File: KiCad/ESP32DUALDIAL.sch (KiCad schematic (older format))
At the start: 53 parts, among them J1 SERVICE, J2 Conn_01x04_Male, J5 Conn_01x03_Male, J6 Conn_01x02_Male, J7 Conn_01x02_Male, J8 Conn_01x02_Male, M1 Fan_CPU_4pin, M2 Fan_CPU_4pin, Q1 Q_NMOS_GDS, SW1 Rotary_Encoder_Switch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

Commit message: change to ROTARY ENCODER chattaling fix. and many change...
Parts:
- added R11, R12, R13, R14, R15, R16: 270, Resistor_SMD:R_0603_1608Metric, symbol Device:R
- added R17, R18, R19, R20, R21, R22: 10k, Resistor_SMD:R_0603_1608Metric, symbol Device:R
- R3: value 4.7k -> 10k
- R5, R6, R7, R8: value 330 -> 270
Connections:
- net +3V3: now also R17.1, R18.1, R19.1, R20.1, R21.1, R22.1
- net OZON0: now also U2.11 (IO26); no longer U2.33 (IO21)
- net PUMP: now also U2.12 (IO27); no longer R1.2, U2.23 (IO15), U4.2 (IO)
- net at C8.1, SW1.A: now also R13.1; no longer U2.12 (IO27)
- net at C9.1, SW1.B: now also R12.1; no longer U2.11 (IO26)
- net at C4.1, SW1.S2: now also R11.1; no longer U2.10 (IO25)
- net at C12.1, SW2.S2: now also R14.1; no longer U2.13 (IO14)
- net at C7.1, SW2.B: now also R15.1; no longer U2.14 (IO12)
- net at C5.1, SW2.A: now also R16.1; no longer U2.16 (IO13)
- net at U2.6 (IO34): now also R12.2, R18.2
- net at U2.7 (IO35): now also R13.2, R20.2
- new net: R1.2, U2.23 (IO15), U4.2 (IO)
- new net: R11.2, R17.2, U2.10 (IO25)
- new net: R14.2, R22.2, U2.13 (IO14)
- new net: R15.2, R19.2, U2.14 (IO12)
- new net: R16.2, R21.2, U2.16 (IO13)
- no-connect marks 30 -> 28
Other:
- moved on the sheet: C5, C7, C8, C9

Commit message: Ver.6 : Add test pads / NNC and SHARP SSR both support / mode jumper
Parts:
- added J3: mode, Connector_PinHeader_2.54mm:PinHeader_2x01_P2.54mm_Vertical, symbol Connector_Generic:Conn_01x02
- added TP1, TP10, TP11, TP12, TP2, TP3, TP4, TP5, TP6, TP8, TP9: TestPoint, TestPoint:TestPoint_Pad_D2.0mm, symbol Connector:TestPoint
- added TP13, TP7: TestPoint, TestPoint:TestPoint_Pad_D3.0mm, symbol Connector:TestPoint
- BZ1: footprint Buzzer_Beeper:Buzzer_12x9.5RM7.6 -> library:Buzzer_7.6_5.0
- U5, U6, U7, U8: footprint library:SSR_SHARP_S108T02 -> library:SSR_SHARP_S108T02_NNC_NNG1D-25mm
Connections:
- net +12V: now also TP13.1
- net +3V3: now also TP7.1
- net GND: now also J3.1 (Pin_1)
- net at R11.2, R17.2, U2.10 (IO25): now also TP1.1
- net at R14.2, R22.2, U2.13 (IO14): now also TP4.1
- net at R15.2, R19.2, U2.14 (IO12): now also TP5.1
- net at R16.2, R21.2, U2.16 (IO13): now also TP6.1
- net at U2.33 (IO21): now also J3.2 (Pin_2)
- net at R12.2, R18.2, U2.6 (IO34): now also TP2.1
- net at R13.2, R20.2, U2.7 (IO35): now also TP3.1
- net at R5.1, U5.3: now also TP9.1
- net at R6.1, U6.3: now also TP10.1
- net at R7.1, U7.3: now also TP11.1
- net at R8.1, U8.3: now also TP12.1
- net at C11.1, D1.2 (A), M1.1 (-)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: now also TP8.1
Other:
- note added: "DO NOT USE R19"
- note added: "SENSOR_VP is GPIO36\nSENSOR_VN is GPIO39\nIO34 to IO39 are input only\nBoot mode is GPIO0,2,4,5,12,15"
- note added: "normally 12V"
- note removed: "IO34,IO35 is input only"
- moved on the sheet: F1, J2, J5, J6, J7, J8, PS1, R5, R6, R7, R8, U5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

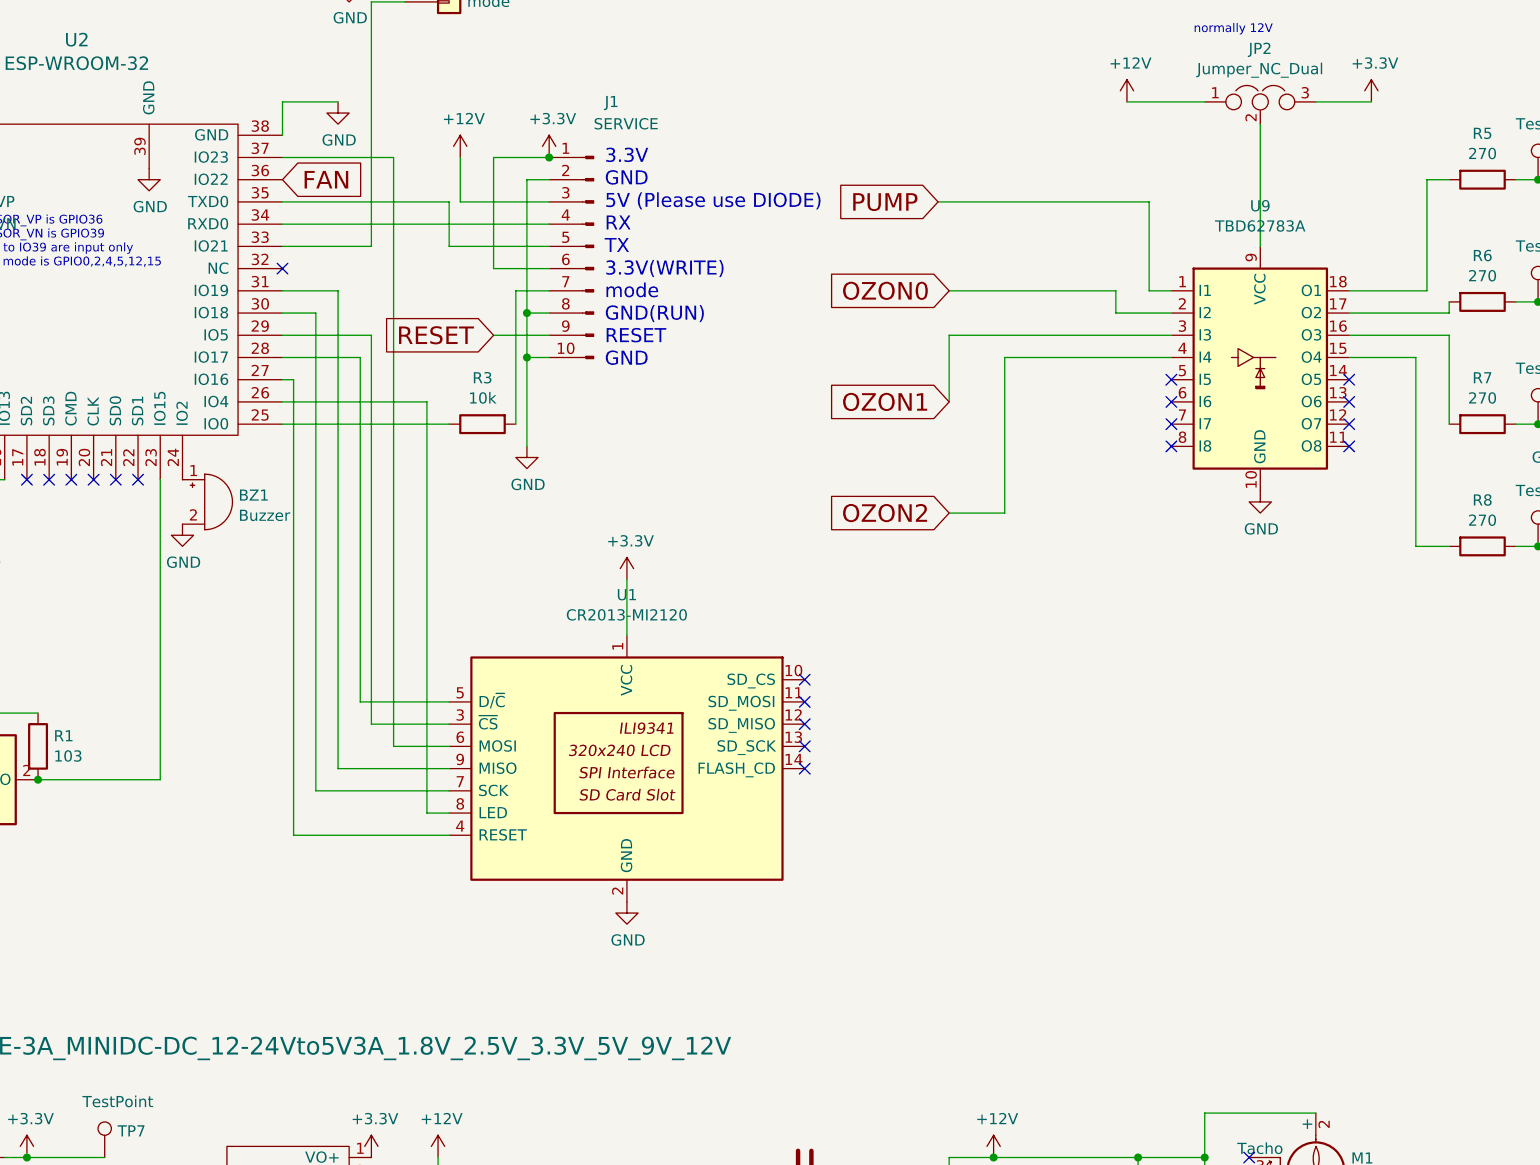
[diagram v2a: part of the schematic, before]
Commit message: Version6 release. Testpad add and follow more SSR type.
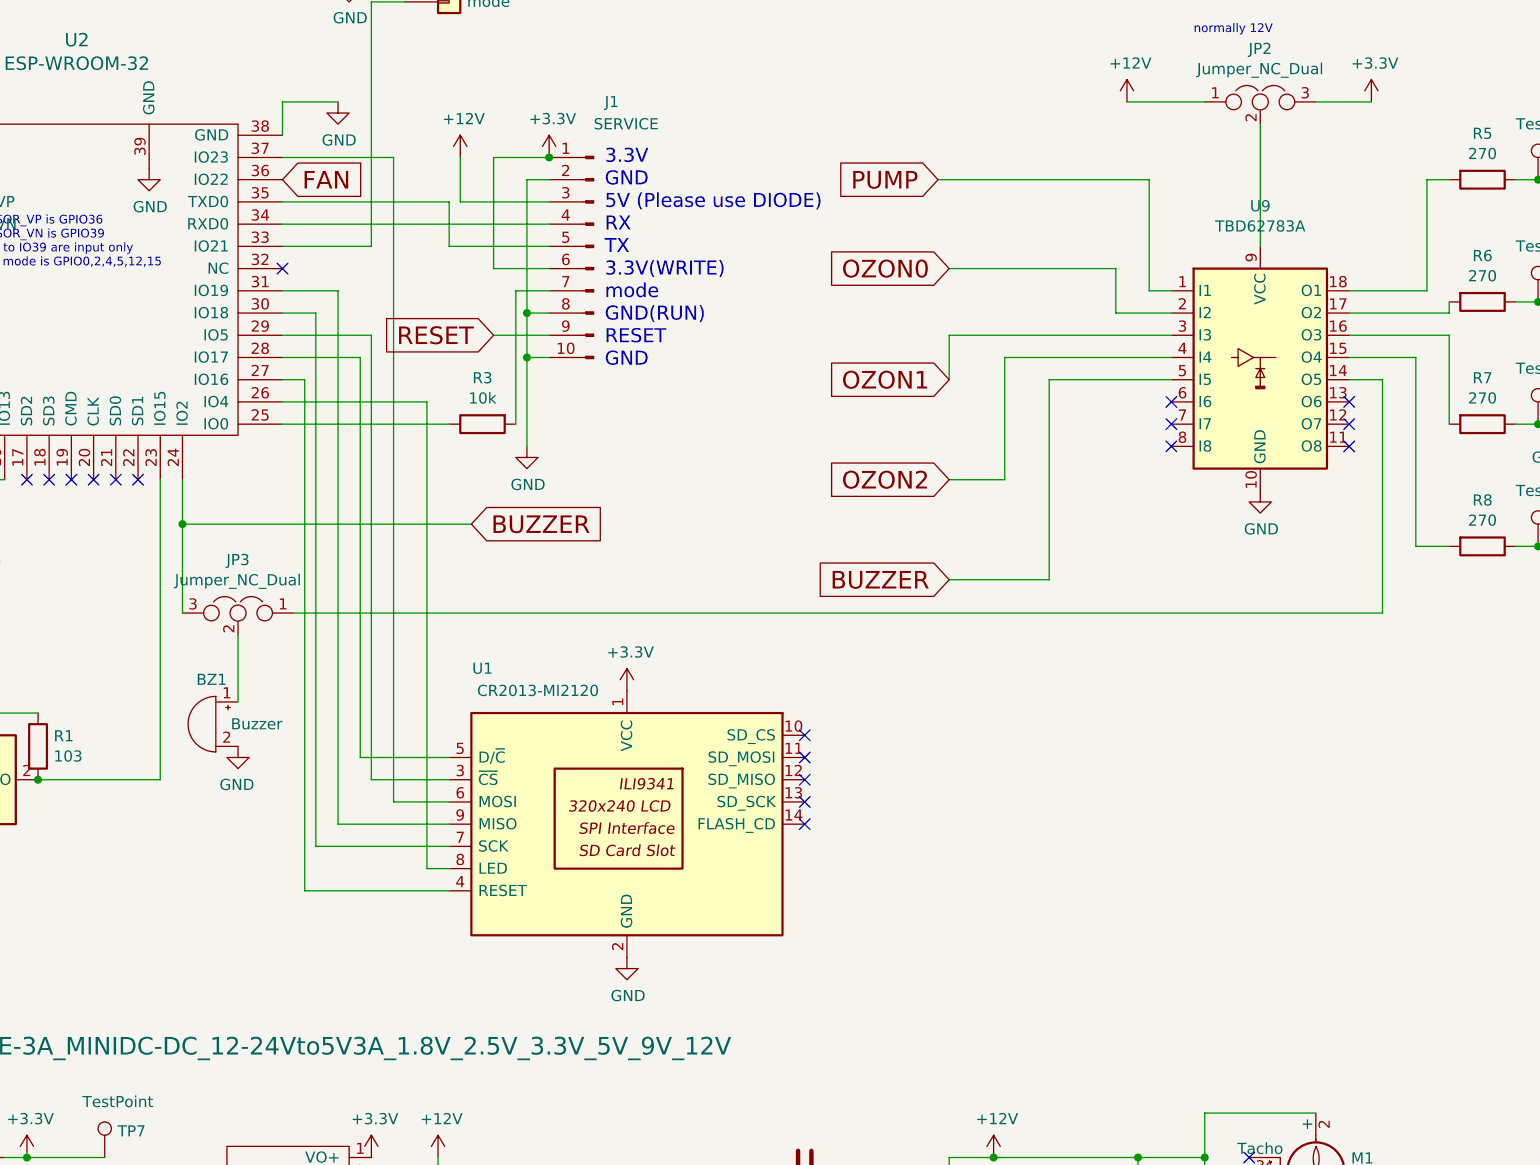
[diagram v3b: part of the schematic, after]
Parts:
- added JP3: Jumper_NC_Dual, Jumper:SolderJumper-3_P1.3mm_Bridged12_RoundedPad1.0x1.5mm_NumberLabels, symbol Device:Jumper_NC_Dual
- Q1: footprint Package_TO_SOT_THT:TO-220-3_Vertical -> Package_TO_SOT_SMD:TO-252-2
- U9: footprint Package_DIP:DIP-18_W7.62mm -> Package_SO:SOIC-18W_7.5x11.6mm_P1.27mm
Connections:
- net at BZ1.1 (-): now also JP3.2; no longer U2.24 (IO2)
- net at U9.14 (O5): now also JP3.1
- net BUZZER: now reaches U9.5 (I5)
- net BUZZER: now also U2.24 (IO2), JP3.3
- no-connect marks 28 -> 26
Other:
- moved on the sheet: BZ1, U1
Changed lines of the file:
@@
 L Driver_Display:CR2013-MI2120 U1
 U 1 1 5DEAE4F9
-P 9000 6050
-F 0 "U1" H 9000 6831 50  0000 C CNN
-F 1 "CR2013-MI2120" H 9000 6740 50  0000 C CNN
-F 2 "library:TFT3.2_ILI9341" H 9000 5350 50  0001 C CNN
-F 3 "http://pan.baidu.com/s/11Y990" H 8350 6550 50  0001 C CNN
-	1    9000 6050
+P 9000 6300
+F 0 "U1" H 9650 7000 50  0000 C CNN
+F 1 "CR2013-MI2120" H 9400 6900 50  0000 C CNN
+F 2 "library:TFT3.2_ILI9341" H 9000 5600 50  0001 C CNN
+F 3 "http://pan.baidu.com/s/11Y990" H 8350 6800 50  0001 C CNN
+	1    9000 6300
 	-1   0    0    -1
 $EndComp
@@
 L power:GND #PWR0103
 U 1 1 5DEE0A3D
-P 9000 6650
-F 0 "#PWR0103" H 9000 6400 50  0001 C CNN
-F 1 "GND" H 9005 6477 50  0000 C CNN
-F 2 "" H 9000 6650 50  0001 C CNN
-F 3 "" H 9000 6650 50  0001 C CNN
-	1    9000 6650
+P 9000 6900
+F 0 "#PWR0103" H 9000 6650 50  0001 C CNN
+F 1 "GND" H 9005 6727 50  0000 C CNN
+F 2 "" H 9000 6900 50  0001 C CNN
+F 3 "" H 9000 6900 50  0001 C CNN
+	1    9000 6900
 	1    0    0    -1
 $EndComp
@@
 L power:+3.3V #PWR0104
 U 1 1 5DEE0A47
-P 9000 5200
-F 0 "#PWR0104" H 9000 5050 50  0001 C CNN
-F 1 "+3.3V" H 9015 5373 50  0000 C CNN
-F 2 "" H 9000 5200 50  0001 C CNN
-F 3 "" H 9000 5200 50  0001 C CNN
-	1    9000 5200
+P 9000 5700
+F 0 "#PWR0104" H 9000 5550 50  0001 C CNN
+F 1 "+3.3V" H 9015 5873 50  0000 C CNN
+F 2 "" H 9000 5700 50  0001 C CNN
+F 3 "" H 9000 5700 50  0001 C CNN
+	1    9000 5700
 	1    0    0    -1
 $EndComp
@@
 $EndComp
 Wire Wire Line
-	9000 5200 9000 5450
-Wire Wire Line
 	1650 4300 1900 4300
 Wire Wire Line
@@
 Wire Wire Line
 	1950 4950 1950 5200
-NoConn ~ 9800 5650
-NoConn ~ 9800 5750
-NoConn ~ 9800 5850
-NoConn ~ 9800 5950
-NoConn ~ 9800 6050
+NoConn ~ 9800 5900
+NoConn ~ 9800 6000
+NoConn ~ 9800 6100
+NoConn ~ 9800 6200
+NoConn ~ 9800 6300
 $Comp
 L Sensor:DHT11 U4
@@
 Connection ~ 6050 5800
 Wire Wire Line
-	7700 6050 8200 6050
+	7700 6300 8200 6300
 $Comp
 L Converter_ACDC:IRM-20-12 PS1
@@
 	7450 3300 7950 3300
 Wire Wire Line
-	7850 5850 7850 4100
+	7850 6100 7850 4100
 Wire Wire Line
 	7850 4100 7450 4100
 Wire Wire Line
-	7850 5850 8200 5850
-Wire Wire Line
-	7800 4200 7800 5750
+	7850 6100 8200 6100
+Wire Wire Line
+	7800 4200 7800 6000
 Wire Wire Line
 	7450 3900 7700 3900
@@
 	7450 4000 7600 4000
 Wire Wire Line
-	7600 4000 7600 6150
-Wire Wire Line
-	7600 6150 8200 6150
-Wire Wire Line
-	7450 4300 7500 4300
-Wire Wire Line
-	7500 4300 7500 6350
-Wire Wire Line
-	7500 6350 8200 6350
+	7600 4000 7600 6400
+Wire Wire Line
+	7600 6400 8200 6400
 Wire Wire Line
 	7450 4400 8100 4400
 Wire Wire Line
-	8100 4400 8100 6250
-Wire Wire Line
-	8100 6250 8200 6250
+	8100 4400 8100 6500
+Wire Wire Line
+	8100 6500 8200 6500
 $Comp
 L power:GND #PWR0114
@@
 Text Notes 15700 4150 0    55   ~ 0
 \nOZON0A\nOZON0B\n\nOZON1A\nOZON1B\n\nOZON2A\nOZON2B
-Text GLabel 10400 3500 0    79   Input ~ 0
+Text GLabel 10400 3400 0    79   Input ~ 0
 PUMP
-Text GLabel 10450 3900 0    79   Input ~ 0
+Text GLabel 10450 3800 0    79   Input ~ 0
 OZON0
-Text GLabel 10450 4400 0    79   Input ~ 0
+Text GLabel 10450 4300 0    79   Input ~ 0
 OZON1
-Text GLabel 10450 4900 0    79   Input ~ 0
+Text GLabel 10450 4750 0    79   Input ~ 0
 OZON2
 $Comp
@@
 	7450 4200 7800 4200
 Wire Wire Line
-	7700 3900 7700 6050
+	7700 3900 7700 6300
 Wire Wire Line
 	6350 6100 6900 6100
@@
 F 0 "U9" H 11850 4881 50  0000 C CNN
 F 1 "TBD62783A" H 11850 4790 50  0000 C CNN
-F 2 "Package_DIP:DIP-18_W7.62mm" H 11850 3650 50  0001 C CNN
+F 2 "Package_SO:SOIC-18W_7.5x11.6mm_P1.27mm" H 11850 3650 50  0001 C CNN
 F 3 "http://toshiba.semicon-storage.com/info/docget.jsp?did=30523&prodName=TBD62783APG" H 11550 4600 50  0001 C CNN
 	1    11850 4200
@@
 Wire Wire Line
 	12250 4100 12700 4100
-NoConn ~ 12250 4300
 NoConn ~ 12250 4400
 NoConn ~ 12250 4500
@@
 NoConn ~ 11450 4500
 NoConn ~ 11450 4400
-NoConn ~ 11450 4300
 Wire Wire Line
 	11450 4000 11200 4000
@@
 F 0 "Q1" H 10804 8396 50  0000 L CNN
 F 1 "Q_NMOS_GDS" H 10804 8305 50  0000 L CNN
-F 2 "Package_TO_SOT_THT:TO-220-3_Vertical" H 10800 8450 50  0001 C CNN
+F 2 "Package_TO_SOT_SMD:TO-252-2" H 10800 8450 50  0001 C CNN
 F 3 "~" H 10600 8350 50  0001 C CNN
 	1    10600 8350
@@
 PUMPA\n\nPUMPB\n
 Wire Wire Line
-	10450 4900 10700 4900
-Wire Wire Line
-	11350 3500 11350 3900
-Wire Wire Line
 	11350 3900 11450 3900
-Wire Wire Line
-	11200 3900 11200 4000
-Wire Wire Line
-	10450 4100 10450 4400
-Wire Wire Line
-	10700 4200 10700 4900
 Wire Wire Line
 	10700 4200 11450 4200
@@
 SENSOR_VP is GPIO36\nSENSOR_VN is GPIO39\nIO34 to IO39 are input only\nBoot mode is GPIO0,2,4,5,12,15
 Wire Wire Line
-	7950 5950 8200 5950
-Wire Wire Line
-	7800 5750 8200 5750
-Wire Wire Line
-	7950 3300 7950 5950
+	7950 6200 8200 6200
+Wire Wire Line
+	7800 6000 8200 6000
+Wire Wire Line
+	7950 3300 7950 6200
 $Comp
 L nanbuwks:Mini560_DC-DC_JW5068A U10
@@
 L power:GND #PWR0130
 U 1 1 5FB938A2
-P 7000 4950
-F 0 "#PWR0130" H 7000 4700 50  0001 C CNN
-F 1 "GND" H 7005 4777 50  0000 C CNN
-F 2 "" H 7000 4950 50  0001 C CNN
-F 3 "" H 7000 4950 50  0001 C CNN
-	1    7000 4950
-	1    0    0    -1
+P 7250 5950
+F 0 "#PWR0130" H 7250 5700 50  0001 C CNN
+F 1 "GND" H 7255 5777 50  0000 C CNN
+F 2 "" H 7250 5950 50  0001 C CNN
+F 3 "" H 7250 5950 50  0001 C CNN
+	1    7250 5950
+	-1   0    0    -1
 $EndComp
 $Comp
 L Device:Buzzer BZ1
 U 1 1 5FB92E0A
-P 7100 4850
-F 0 "BZ1" H 7252 4879 50  0000 L CNN
-F 1 "Buzzer" H 7252 4788 50  0000 L CNN
-F 2 "library:Buzzer_7.6_5.0" V 7075 4950 50  0001 C CNN
-F 3 "~" V 7075 4950 50  0001 C CNN
-	1    7100 4850
-	1    0    0    -1
+P 7150 5850
+F 0 "BZ1" H 7100 6050 50  0000 L CNN
+F 1 "Buzzer" H 6850 5850 50  0000 L CNN
+F 2 "library:Buzzer_7.6_5.0" V 7125 5950 50  0001 C CNN
+F 3 "~" V 7125 5950 50  0001 C CNN
+	1    7150 5850
+	-1   0    0    -1
 $EndComp
 Wire Wire Line
@@
 Text Notes 11550 2750 0    39   ~ 0
 normally 12V
-Wire Wire Line
-	10450 4100 11450 4100
-Wire Wire Line
-	10450 3900 11200 3900
-Wire Wire Line
-	10400 3500 11350 3500
 $Comp
 L Connector:TestPoint TP9
@@
 	1    0    0    -1
 $EndComp
+$Comp
+L Device:Jumper_NC_Dual JP3
+U 1 1 6100F97B
+P 7250 5350
+F 0 "JP3" H 7250 5589 50  0000 C CNN
+F 1 "Jumper_NC_Dual" H 7250 5498 50  0000 C CNN
+F 2 "Jumper:SolderJumper-3_P1.3mm_Bridged12_RoundedPad1.0x1.5mm_NumberLabels" H 7250 5350 50  0001 C CNN
+F 3 "~" H 7250 5350 50  0001 C CNN
+	1    7250 5350
+	-1   0    0    -1
+$EndComp
+Wire Wire Line
+	7550 4300 7550 6600
+Wire Wire Line
+	7550 6600 8200 6600
+Wire Wire Line
+	7450 4300 7550 4300
+Wire Wire Line
+	7250 5450 7250 5750
+Wire Wire Line
+	7000 5350 7000 4950
+Wire Wire Line
+	7000 4950 8300 4950
+Connection ~ 7000 4950
+Wire Wire Line
+	7000 4950 7000 4750
+Wire Wire Line
+	10700 4200 10700 4750
+Wire Wire Line
+	11450 4300 10900 4300
+Text GLabel 10450 5200 0    79   Input ~ 0
+BUZZER
+Text GLabel 8300 4950 2    79   Input ~ 0
+BUZZER
+Wire Wire Line
+	7500 5350 12400 5350
+Wire Wire Line
+	12400 5350 12400 4300
+Wire Wire Line
+	12400 4300 12250 4300
+Wire Wire Line
+	10450 4100 11450 4100
+Wire Wire Line
+	10450 4100 10450 4300
+Wire Wire Line
+	10450 4750 10700 4750
+Wire Wire Line
+	10450 5200 10900 5200
+Wire Wire Line
+	10900 4300 10900 5200
+Wire Wire Line
+	11200 3800 11200 4000
+Wire Wire Line
+	11200 3800 10450 3800
+Wire Wire Line
+	11350 3400 11350 3900
+Wire Wire Line
+	10400 3400 11350 3400
 $EndSCHEMATC
